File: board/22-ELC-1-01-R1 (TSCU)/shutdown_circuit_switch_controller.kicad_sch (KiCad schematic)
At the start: 26 parts, among them Q10 AO3400A, Q11 SUD50P04-09L-E3, Q12 SUD50P04-09L-E3, Q9 AO3400A, SW1 FAULT_RESET, U7 74HC74D,653, U8 SGM809-SXN3/TR

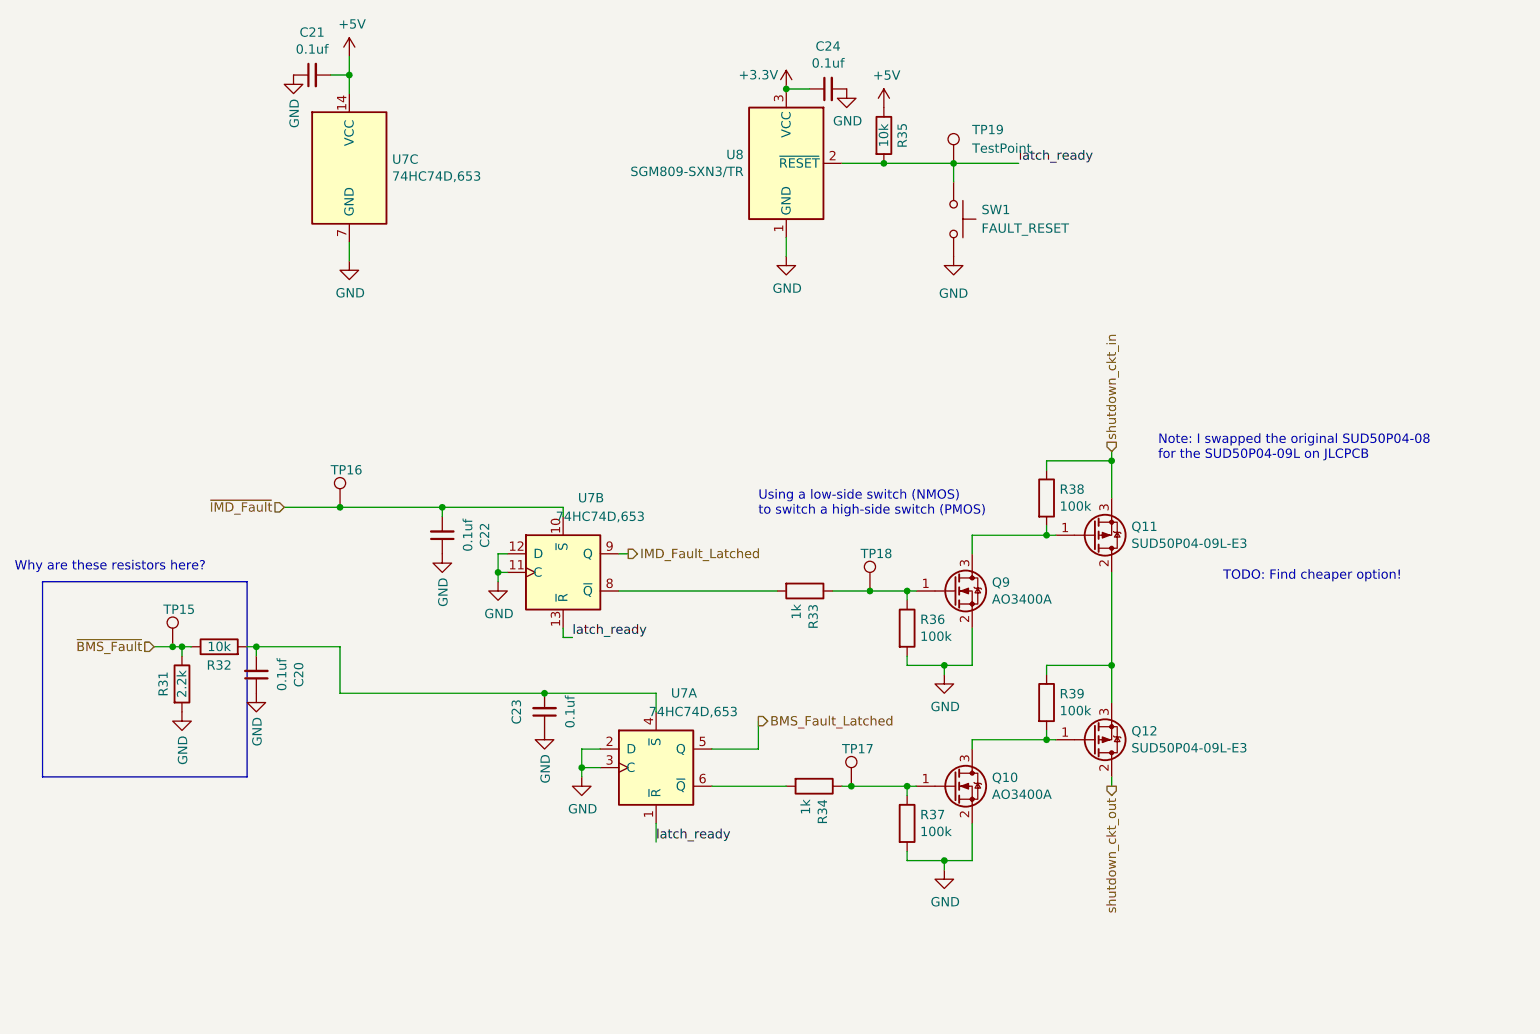
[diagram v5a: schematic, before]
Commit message: Finalized schematic, started board layout
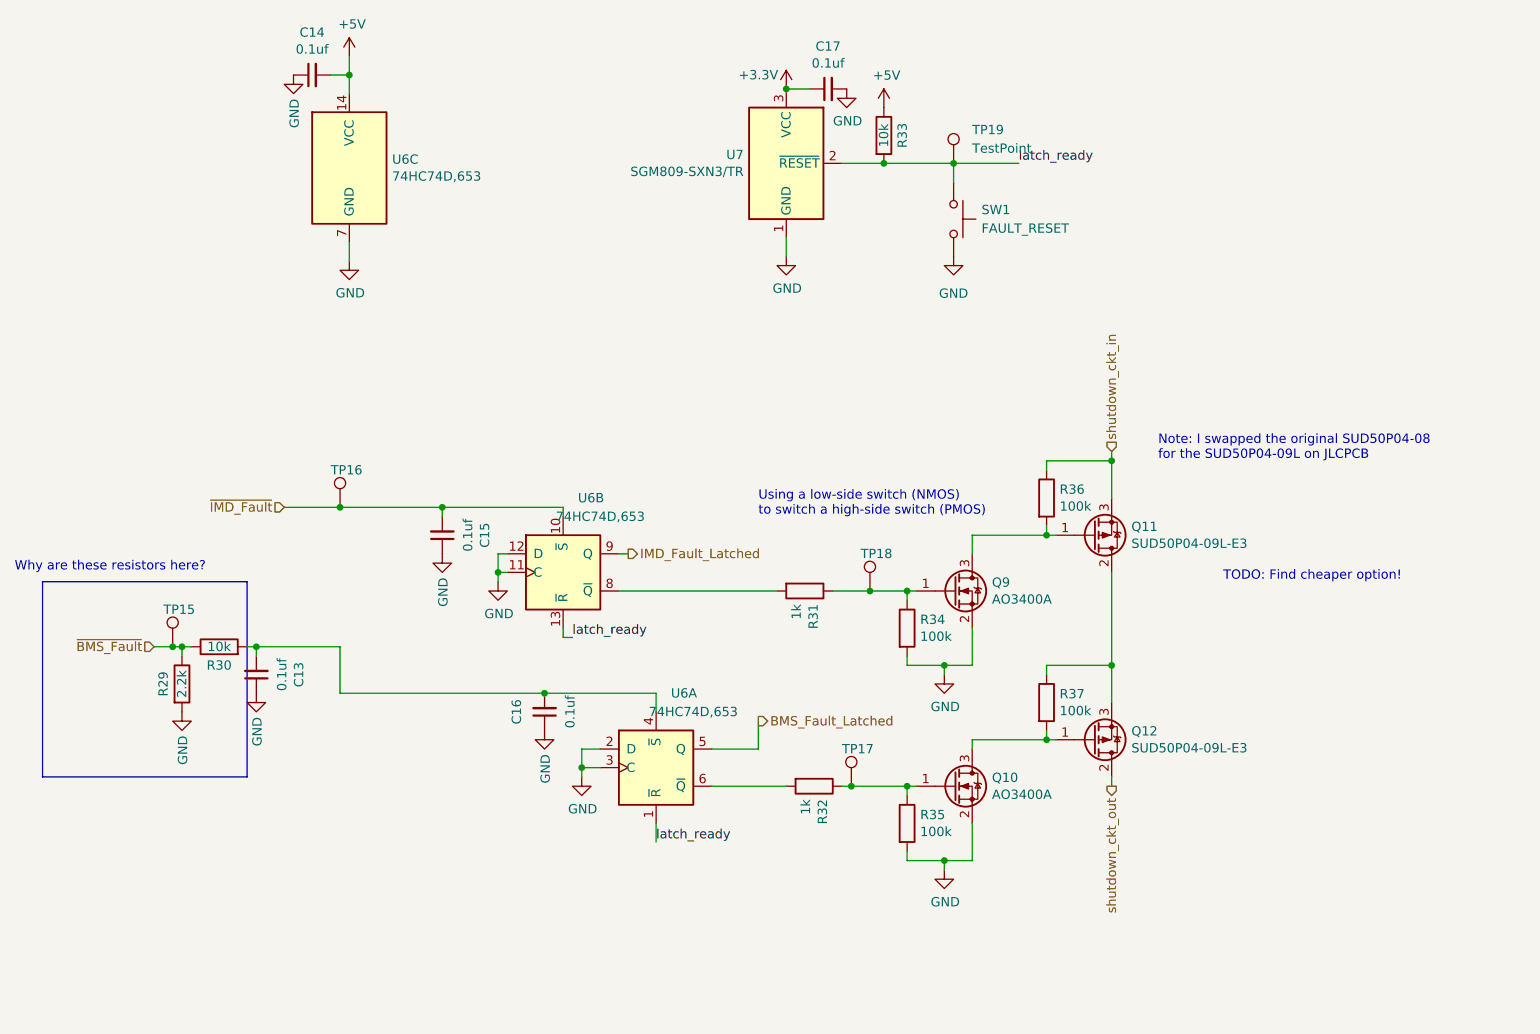
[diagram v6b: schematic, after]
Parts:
- C13: renamed from C20; footprint Capacitor_SMD:C_0603_1608Metric_Pad1.08x0.95mm_HandSolder -> Capacitor_SMD:C_0402_1005Metric
- C14: renamed from C21; footprint Capacitor_SMD:C_0603_1608Metric_Pad1.08x0.95mm_HandSolder -> Capacitor_SMD:C_0402_1005Metric
- C15: renamed from C22; footprint Capacitor_SMD:C_0603_1608Metric_Pad1.08x0.95mm_HandSolder -> Capacitor_SMD:C_0402_1005Metric
- C16: renamed from C23; footprint Capacitor_SMD:C_0603_1608Metric_Pad1.08x0.95mm_HandSolder -> Capacitor_SMD:C_0402_1005Metric
- C17: renamed from C24; footprint Capacitor_SMD:C_0603_1608Metric_Pad1.08x0.95mm_HandSolder -> Capacitor_SMD:C_0402_1005Metric
- R29: renamed from R31; footprint Resistor_SMD:R_0603_1608Metric_Pad0.98x0.95mm_HandSolder -> FixedTextSizes:R_0402_1005Metric
- R30: renamed from R32; footprint Resistor_SMD:R_0603_1608Metric_Pad0.98x0.95mm_HandSolder -> FixedTextSizes:R_0402_1005Metric
- R31: renamed from R33; footprint Resistor_SMD:R_0603_1608Metric_Pad0.98x0.95mm_HandSolder -> FixedTextSizes:R_0402_1005Metric
- R32: renamed from R34; footprint Resistor_SMD:R_0603_1608Metric_Pad0.98x0.95mm_HandSolder -> FixedTextSizes:R_0402_1005Metric
- R33: renamed from R35; footprint Resistor_SMD:R_0603_1608Metric_Pad0.98x0.95mm_HandSolder -> FixedTextSizes:R_0402_1005Metric
- R34: renamed from R36; footprint Resistor_SMD:R_0603_1608Metric_Pad0.98x0.95mm_HandSolder -> FixedTextSizes:R_0402_1005Metric
- R35: renamed from R37; footprint Resistor_SMD:R_0603_1608Metric_Pad0.98x0.95mm_HandSolder -> FixedTextSizes:R_0402_1005Metric
- R36: renamed from R38; footprint Resistor_SMD:R_0603_1608Metric_Pad0.98x0.95mm_HandSolder -> FixedTextSizes:R_0402_1005Metric
- R37: renamed from R39; footprint Resistor_SMD:R_0603_1608Metric_Pad0.98x0.95mm_HandSolder -> FixedTextSizes:R_0402_1005Metric
- renumbered U7 to U6, U8 to U7

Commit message: More progress
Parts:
- C13, C14, C15, C16, C17: footprint Capacitor_SMD:C_0402_1005Metric -> FixedTextSizes:C_0402_1005Metric_Pad0.74x0.62mm_HandSolder_Reasonable_Text_Size
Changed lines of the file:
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@@
     (property "Reference" "C13" (id 0) (at 50.2666 119.38 90))
     (property "Value" "0.1uf" (id 1) (at 47.9552 119.38 90))
-    (property "Footprint" "Capacitor_SMD:C_0402_1005Metric" (id 2) (at 44.45 119.38 0)
+    (property "Footprint" "FixedTextSizes:C_0402_1005Metric_Pad0.74x0.62mm_HandSolder_Reasonable_Text_Size" (id 2) (at 44.45 119.38 0)
       (effects (font (size 1.27 1.27)) hide)
     )
@@
   (symbol (lib_id "power:GND") (at 44.45 121.92 0) (unit 1)
     (in_bom yes) (on_board yes)
-    (property "Reference" "#PWR066" (id 0) (at 44.45 128.27 0)
+    (property "Reference" "#PWR069" (id 0) (at 44.45 128.27 0)
       (effects (font (size 1.27 1.27)) hide)
     )
@@
   (symbol (lib_id "power:GND") (at 34.29 124.46 0) (unit 1)
     (in_bom yes) (on_board yes)
-    (property "Reference" "#PWR065" (id 0) (at 34.29 130.81 0)
+    (property "Reference" "#PWR068" (id 0) (at 34.29 130.81 0)
       (effects (font (size 1.27 1.27)) hide)
     )
@@
   (symbol (lib_id "power:GND") (at 138.43 119.38 0) (unit 1)
     (in_bom yes) (on_board yes)
-    (property "Reference" "#PWR078" (id 0) (at 138.43 125.73 0)
+    (property "Reference" "#PWR081" (id 0) (at 138.43 125.73 0)
       (effects (font (size 1.27 1.27)) hide)
     )
@@
   (symbol (lib_id "power:GND") (at 138.43 146.05 0) (unit 1)
     (in_bom yes) (on_board yes)
-    (property "Reference" "#PWR079" (id 0) (at 138.43 152.4 0)
+    (property "Reference" "#PWR082" (id 0) (at 138.43 152.4 0)
       (effects (font (size 1.27 1.27)) hide)
     )
@@
   (symbol (lib_id "power:GND") (at 77.47 106.68 0) (unit 1)
     (in_bom yes) (on_board yes)
-    (property "Reference" "#PWR071" (id 0) (at 77.47 113.03 0)
+    (property "Reference" "#PWR074" (id 0) (at 77.47 113.03 0)
       (effects (font (size 1.27 1.27)) hide)
     )
@@
   (symbol (lib_id "power:GND") (at 88.9 133.35 0) (unit 1)
     (in_bom yes) (on_board yes)
-    (property "Reference" "#PWR073" (id 0) (at 88.9 139.7 0)
+    (property "Reference" "#PWR076" (id 0) (at 88.9 139.7 0)
       (effects (font (size 1.27 1.27)) hide)
     )
@@
     (property "Reference" "C15" (id 0) (at 75.6666 100.33 90))
     (property "Value" "0.1uf" (id 1) (at 73.3552 100.33 90))
-    (property "Footprint" "Capacitor_SMD:C_0402_1005Metric" (id 2) (at 69.85 100.33 0)
+    (property "Footprint" "FixedTextSizes:C_0402_1005Metric_Pad0.74x0.62mm_HandSolder_Reasonable_Text_Size" (id 2) (at 69.85 100.33 0)
       (effects (font (size 1.27 1.27)) hide)
     )
@@
   (symbol (lib_id "power:GND") (at 69.85 102.87 0) (unit 1)
     (in_bom yes) (on_board yes)
-    (property "Reference" "#PWR070" (id 0) (at 69.85 109.22 0)
+    (property "Reference" "#PWR073" (id 0) (at 69.85 109.22 0)
       (effects (font (size 1.27 1.27)) hide)
     )
@@
   (symbol (lib_id "power:GND") (at 49.53 37.465 0) (unit 1)
     (in_bom yes) (on_board yes)
-    (property "Reference" "#PWR067" (id 0) (at 49.53 43.815 0)
+    (property "Reference" "#PWR070" (id 0) (at 49.53 43.815 0)
       (effects (font (size 1.27 1.27)) hide)
     )
@@
     (property "Reference" "C14" (id 0) (at 52.07 31.6484 90))
     (property "Value" "0.1uf" (id 1) (at 52.07 33.9598 90))
-    (property "Footprint" "Capacitor_SMD:C_0402_1005Metric" (id 2) (at 52.07 37.465 0)
+    (property "Footprint" "FixedTextSizes:C_0402_1005Metric_Pad0.74x0.62mm_HandSolder_Reasonable_Text_Size" (id 2) (at 52.07 37.465 0)
       (effects (font (size 1.27 1.27)) hide)
     )
@@
   (symbol (lib_id "power:GND") (at 57.15 62.865 0) (unit 1)
     (in_bom yes) (on_board yes)
-    (property "Reference" "#PWR069" (id 0) (at 57.15 69.215 0)
+    (property "Reference" "#PWR072" (id 0) (at 57.15 69.215 0)
       (effects (font (size 1.27 1.27)) hide)
     )
@@
   (symbol (lib_id "power:+3.3V") (at 116.84 39.37 0) (unit 1)
     (in_bom yes) (on_board yes)
-    (property "Reference" "#PWR074" (id 0) (at 116.84 43.18 0)
+    (property "Reference" "#PWR077" (id 0) (at 116.84 43.18 0)
       (effects (font (size 1.27 1.27)) hide)
     )
@@
   (symbol (lib_id "power:GND") (at 116.84 62.23 0) (unit 1)
     (in_bom yes) (on_board yes)
-    (property "Reference" "#PWR075" (id 0) (at 116.84 68.58 0)
+    (property "Reference" "#PWR078" (id 0) (at 116.84 68.58 0)
       (effects (font (size 1.27 1.27)) hide)
     )
@@
     (property "Reference" "C17" (id 0) (at 122.555 33.5534 90))
     (property "Value" "0.1uf" (id 1) (at 122.555 35.8648 90))
-    (property "Footprint" "Capacitor_SMD:C_0402_1005Metric" (id 2) (at 122.555 39.37 0)
+    (property "Footprint" "FixedTextSizes:C_0402_1005Metric_Pad0.74x0.62mm_HandSolder_Reasonable_Text_Size" (id 2) (at 122.555 39.37 0)
       (effects (font (size 1.27 1.27)) hide)
     )
@@
   (symbol (lib_id "power:GND") (at 125.095 39.37 0) (unit 1)
     (in_bom yes) (on_board yes)
-    (property "Reference" "#PWR076" (id 0) (at 125.095 45.72 0)
+    (property "Reference" "#PWR079" (id 0) (at 125.095 45.72 0)
       (effects (font (size 1.27 1.27)) hide)
     )
@@
   (symbol (lib_id "power:+5V") (at 57.15 34.925 0) (unit 1)
     (in_bom yes) (on_board yes)
-    (property "Reference" "#PWR068" (id 0) (at 57.15 38.735 0)
+    (property "Reference" "#PWR071" (id 0) (at 57.15 38.735 0)
       (effects (font (size 1.27 1.27)) hide)
     )
@@
   (symbol (lib_id "power:+5V") (at 130.175 41.91 0) (unit 1)
     (in_bom yes) (on_board yes)
-    (property "Reference" "#PWR077" (id 0) (at 130.175 45.72 0)
+    (property "Reference" "#PWR080" (id 0) (at 130.175 45.72 0)
       (effects (font (size 1.27 1.27)) hide)
     )
@@
   (symbol (lib_id "power:GND") (at 83.82 127 0) (unit 1)
     (in_bom yes) (on_board yes)
-    (property "Reference" "#PWR072" (id 0) (at 83.82 133.35 0)
+    (property "Reference" "#PWR075" (id 0) (at 83.82 133.35 0)
       (effects (font (size 1.27 1.27)) hide)
     )
@@
     (property "Reference" "C16" (id 0) (at 80.01 124.46 90))
     (property "Value" "0.1uf" (id 1) (at 87.3252 124.46 90))
-    (property "Footprint" "Capacitor_SMD:C_0402_1005Metric" (id 2) (at 83.82 124.46 0)
+    (property "Footprint" "FixedTextSizes:C_0402_1005Metric_Pad0.74x0.62mm_HandSolder_Reasonable_Text_Size" (id 2) (at 83.82 124.46 0)
       (effects (font (size 1.27 1.27)) hide)
     )
@@
   (symbol (lib_id "power:GND") (at 139.7 62.23 0) (unit 1)
     (in_bom yes) (on_board yes) (fields_autoplaced)
-    (property "Reference" "#PWR080" (id 0) (at 139.7 68.58 0)
-      (effects (font (size 1.27 1.27)) hide)
-    )
+    (property "Reference" "#PWR083" (id 0) (at 139.7 68.58 0)
+      (effects (font (size 1.27 1.27)) hide)
+    )
